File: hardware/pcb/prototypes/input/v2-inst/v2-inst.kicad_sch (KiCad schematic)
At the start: 42 parts, among them J1 PH, J2 ANLG, J3 LOWV, J4 GND, J5 TRS, J6 XLR, J7 SW CTRL, J8 OUT_BIAS, J9 OUT, SW1 DG1412EEQ, U1 OPA1641, U2 OPA1612AxD, U3 OPA1637

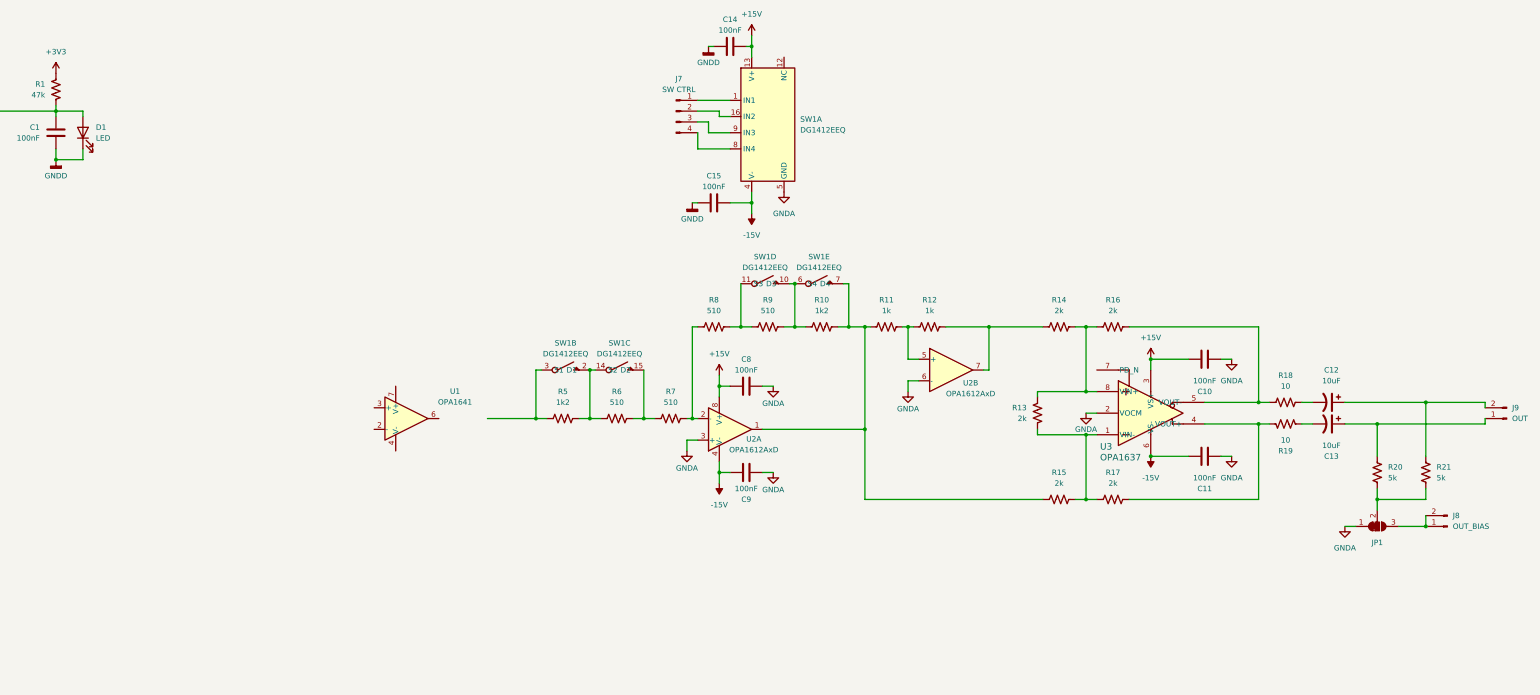
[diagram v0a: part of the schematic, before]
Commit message: create inst input from line
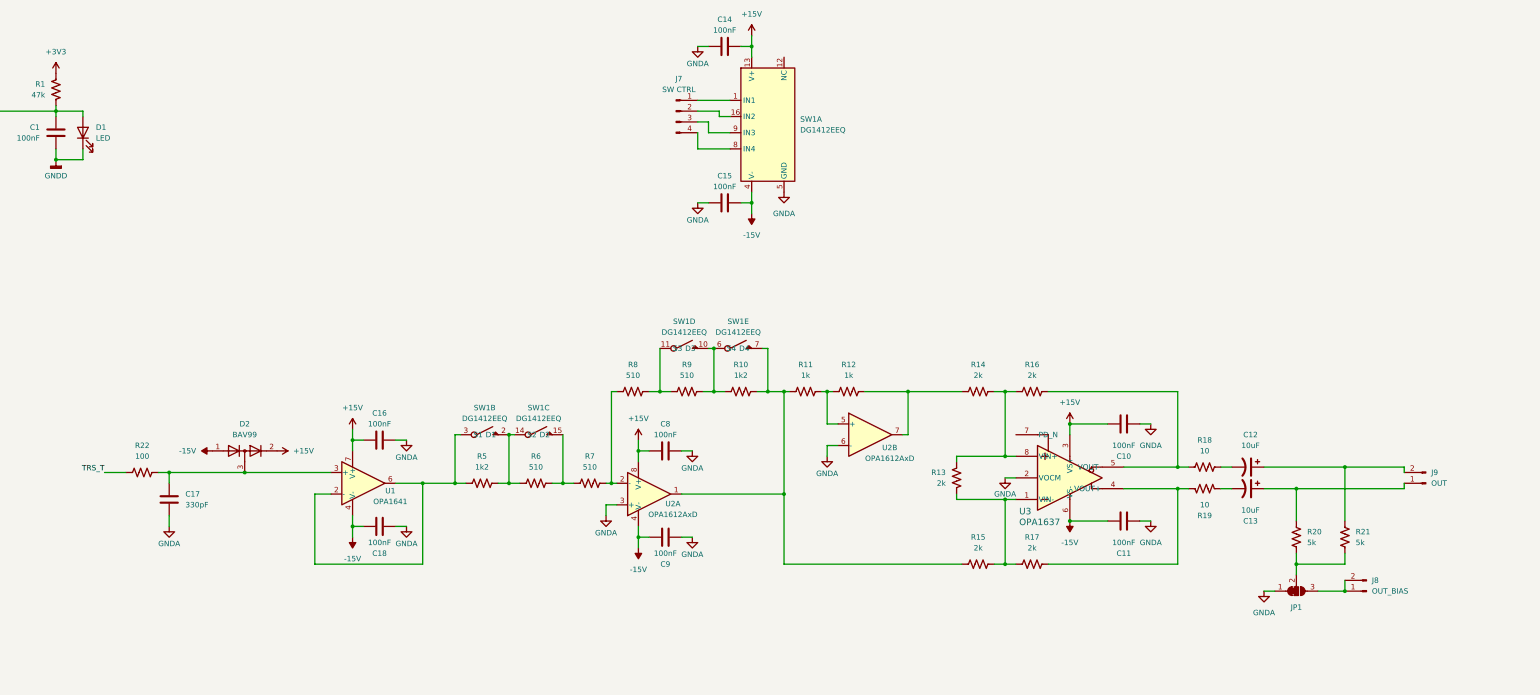
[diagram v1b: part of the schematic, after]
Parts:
- added C16, C18: 100nF, Capacitor_SMD:C_0805_2012Metric_Pad1.18x1.45mm_HandSolder, symbol Device:C
- added C17: 330pF, Capacitor_SMD:C_0805_2012Metric_Pad1.18x1.45mm_HandSolder, symbol Device:C
- added D2: BAV99, Package_TO_SOT_SMD:SOT-23, symbol Diode:BAV99
- added R22: 100, Resistor_SMD:R_0805_2012Metric_Pad1.20x1.40mm_HandSolder, symbol Device:R_US
- U1: footprint (none) -> Package_SO:SOIC-8_3.9x4.9mm_P1.27mm
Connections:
- net +15V: now also C14.2, U1.7 (V+), C16.2, D2.2 (A); no longer C14.1
- net -15V: now also C15.2, U1.4 (V-), C18.2, D2.1 (K); no longer C15.1
- net Earth: now also C14.1, C15.1, C16.1, C17.2, C18.1; no longer C14.2, C15.2
- net TRS_T: now also R22.2
- net at U1.2 (-): now also R5.2, SW1.3 (S1), U1.6
- net at U1.3 (+): now also C17.1, D2.3 (K), R22.1
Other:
- moved on the sheet: C10, C11, C12, C13, C8, C9, J8, J9, JP1, R10, R11, R12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
